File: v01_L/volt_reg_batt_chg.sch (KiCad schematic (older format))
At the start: 13 parts, among them P13 JST-PH2, Q3 PNP, SW3 DIPS_01, U4 MIC5219

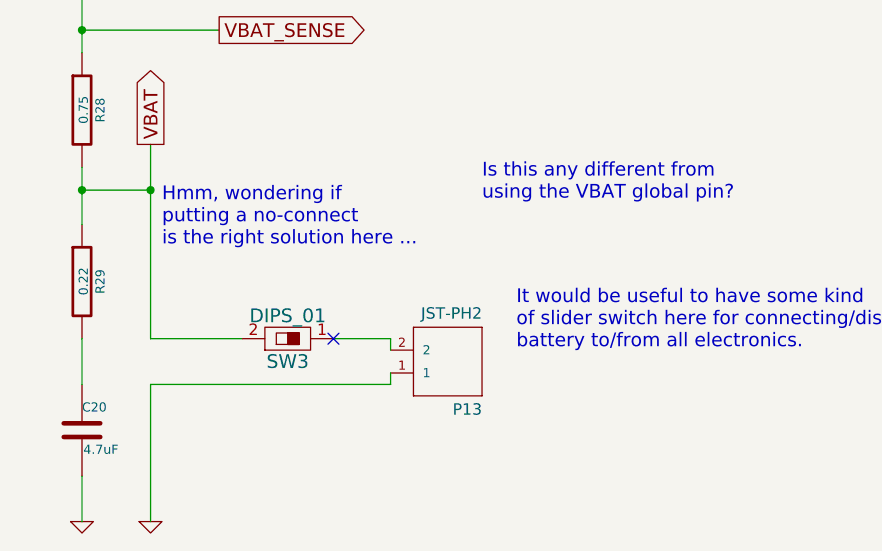
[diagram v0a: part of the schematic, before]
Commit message: Update includes removing right side of audio circuit
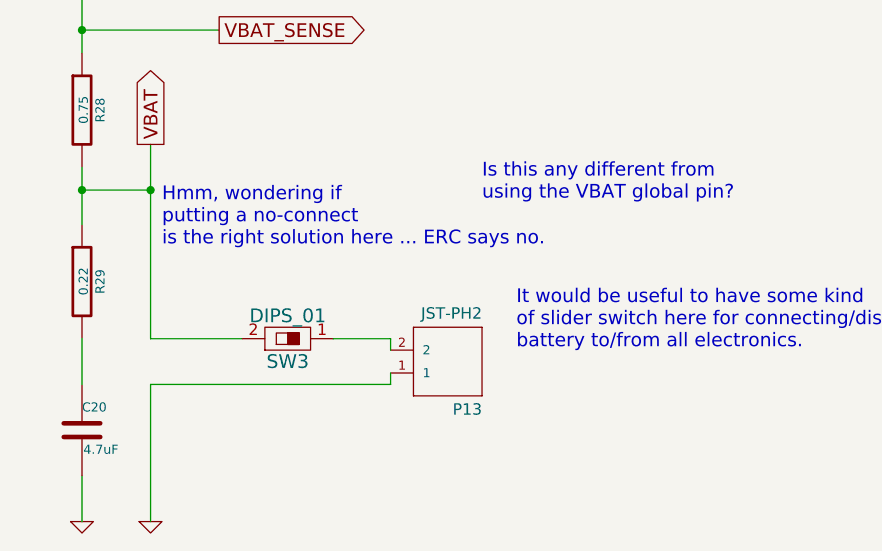
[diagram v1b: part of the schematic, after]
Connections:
- no-connect marks 2 -> 1
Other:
- note added: "Hmm, wondering if \nputting a no-connect\nis the right solution here ... ERC says no."
- note removed: "Hmm, wondering if \nputting a no-connect\nis the right solution here ..."
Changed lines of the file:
@@
 Sheet 4 4
 Title ""
-Date "7 dec 2014"
+Date "16 jan 2015"
 Rev ""
 Comp ""
@@
 $EndComp
 $Comp
-L GND #PWR18
+L GND #PWR013
 U 1 1 5439B1A3
 P 4900 2700
-F 0 "#PWR18" H 4900 2700 30  0001 C CNN
+F 0 "#PWR013" H 4900 2700 30  0001 C CNN
 F 1 "GND" H 4900 2630 30  0001 C CNN
 F 2 "" H 4900 2700 60  0000 C CNN
@@
 $EndComp
 $Comp
-L GND #PWR15
+L GND #PWR014
 U 1 1 5439B578
 P 2250 6250
-F 0 "#PWR15" H 2250 6250 30  0001 C CNN
+F 0 "#PWR014" H 2250 6250 30  0001 C CNN
 F 1 "GND" H 2250 6180 30  0001 C CNN
 F 2 "" H 2250 6250 60  0000 C CNN
@@
 3.3V
 $Comp
-L PWR_FLAG #FLG2
+L PWR_FLAG #FLG015
 U 1 1 5439CBDC
 P 2150 1600
-F 0 "#FLG2" H 2150 1695 30  0001 C CNN
+F 0 "#FLG015" H 2150 1695 30  0001 C CNN
 F 1 "PWR_FLAG" H 2150 1780 30  0000 C CNN
 F 2 "" H 2150 1600 60  0000 C CNN
@@
 $EndComp
 $Comp
-L +BATT #PWR14
+L +BATT #PWR016
 U 1 1 5439CC42
 P 2150 1850
-F 0 "#PWR14" H 2150 1800 20  0001 C CNN
+F 0 "#PWR016" H 2150 1800 20  0001 C CNN
 F 1 "+BATT" H 2150 1950 30  0000 C CNN
 F 2 "" H 2150 1850 60  0000 C CNN
@@
 VIN
 $Comp
-L GND #PWR17
+L GND #PWR017
 U 1 1 5439D063
 P 2550 6250
-F 0 "#PWR17" H 2550 6250 30  0001 C CNN
+F 0 "#PWR017" H 2550 6250 30  0001 C CNN
 F 1 "GND" H 2550 6180 30  0001 C CNN
 F 2 "" H 2550 6250 60  0000 C CNN
@@
 	1850 1600 1850 1850
 $Comp
-L +5V #PWR13
+L +5V #PWR018
 U 1 1 5439CBF7
 P 1850 1850
-F 0 "#PWR13" H 1850 1940 20  0001 C CNN
+F 0 "#PWR018" H 1850 1940 20  0001 C CNN
 F 1 "+5V" H 1850 1940 30  0000 C CNN
 F 2 "" H 1850 1850 60  0000 C CNN
@@
 $EndComp
 $Comp
-L PWR_FLAG #FLG1
+L PWR_FLAG #FLG019
 U 1 1 5439CBEF
 P 1850 1600
-F 0 "#FLG1" H 1850 1695 30  0001 C CNN
+F 0 "#FLG019" H 1850 1695 30  0001 C CNN
 F 1 "PWR_FLAG" H 1850 1780 30  0000 C CNN
 F 2 "" H 1850 1600 60  0000 C CNN
@@
 	2450 1600 2450 1900
 $Comp
-L GND #PWR16
+L GND #PWR020
 U 1 1 5439CC8E
 P 2450 1900
-F 0 "#PWR16" H 2450 1900 30  0001 C CNN
+F 0 "#PWR020" H 2450 1900 30  0001 C CNN
 F 1 "GND" H 2450 1830 30  0001 C CNN
 F 2 "" H 2450 1900 60  0000 C CNN
@@
 $EndComp
 $Comp
-L PWR_FLAG #FLG3
+L PWR_FLAG #FLG021
 U 1 1 5439CBE9
 P 2450 1600
-F 0 "#FLG3" H 2450 1695 30  0001 C CNN
+F 0 "#FLG021" H 2450 1695 30  0001 C CNN
 F 1 "PWR_FLAG" H 2450 1780 30  0000 C CNN
 F 2 "" H 2450 1600 60  0000 C CNN
@@
 	0    -1   -1   0
 $EndComp
-NoConn ~ 3350 5450
 Text Notes 2600 5050 0    60   ~ 0
-Hmm, wondering if \nputting a no-connect\nis the right solution here ...
+Hmm, wondering if \nputting a no-connect\nis the right solution here ... ERC says no.
 $Comp
 L JST-PH2 P13
